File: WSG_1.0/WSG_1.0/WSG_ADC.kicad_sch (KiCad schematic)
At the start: 31 parts, among them J2 USB4110-GF-A, J4 Conn_01x02, U10 TPS22916BYFPR, U11 W25N04KVZEIR, U7 PQ25180YBGT, U8 TPS63802DLAR, U9 TPS7A2025PDBVR

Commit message: finished schematic
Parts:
- added C33: 100nF, symbol Device:C
- added R31: 1M, symbol Device:R
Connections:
- net GND: now also C19.2, C33.2, R31.1
- net VBAT_SENSE: now also C33.1, R31.2
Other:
- moved on the sheet: C19, R26

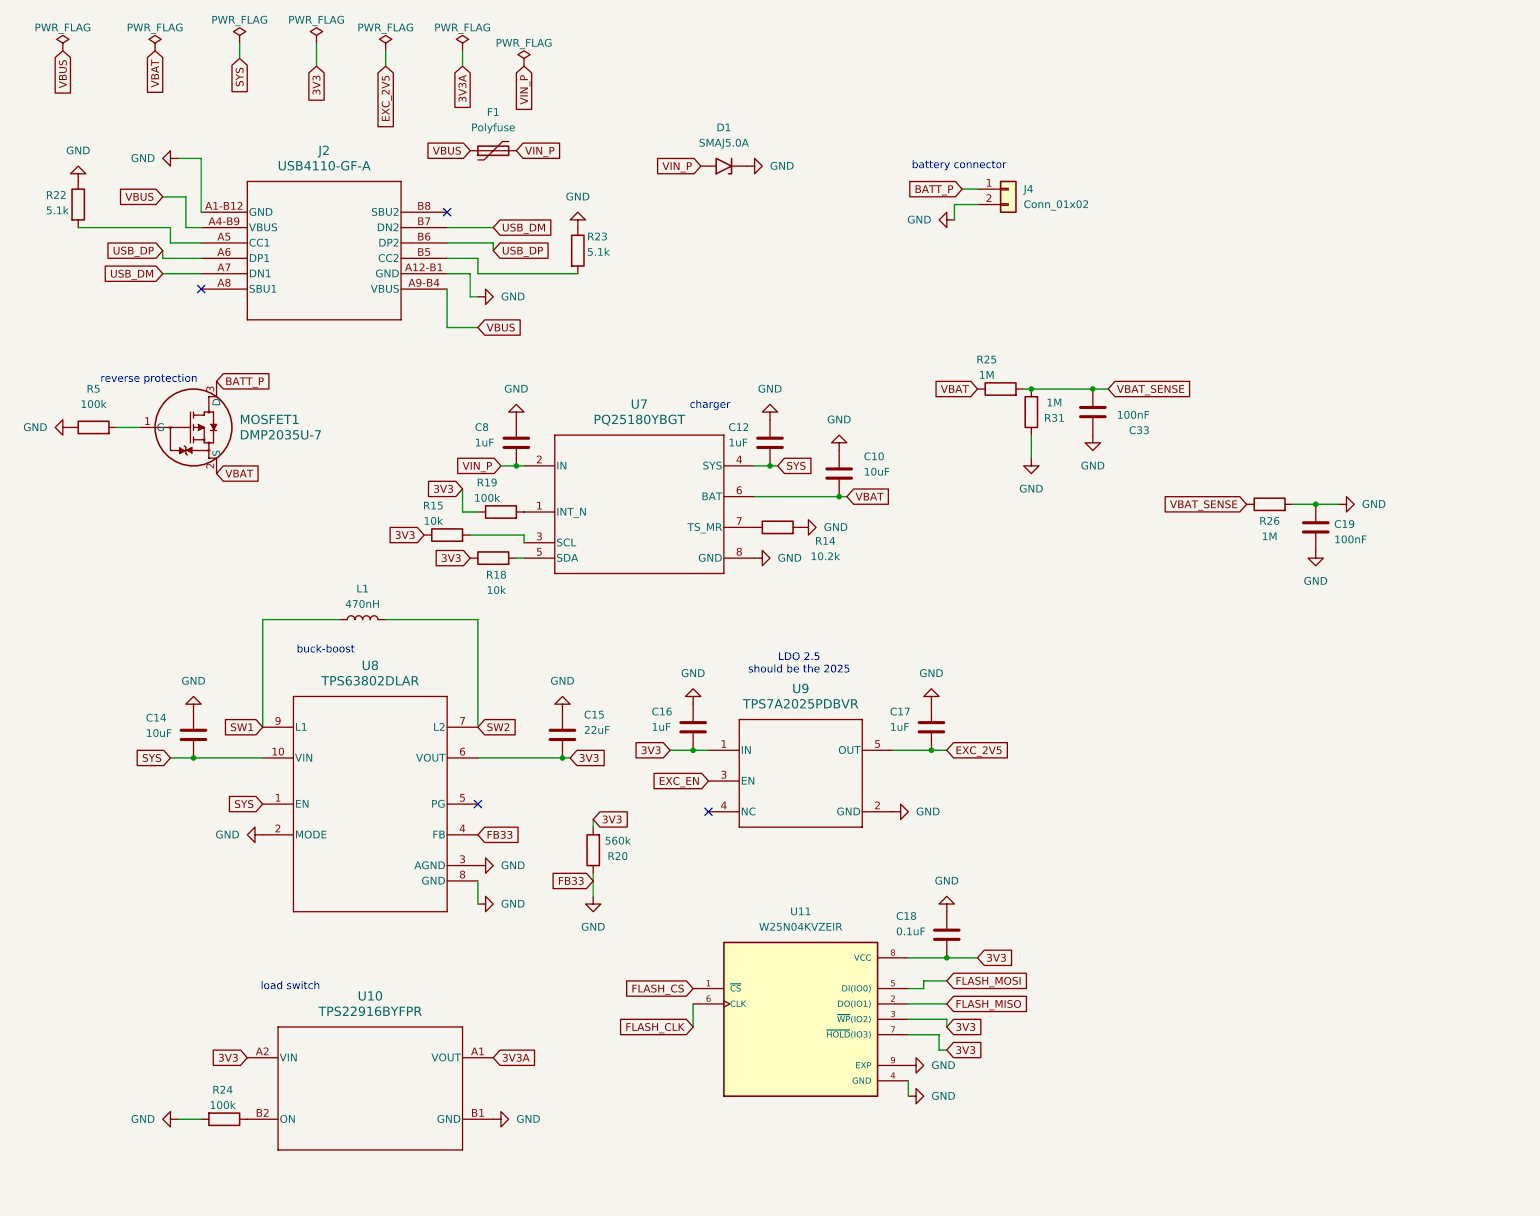
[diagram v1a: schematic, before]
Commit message: added mounting holes, usb esd
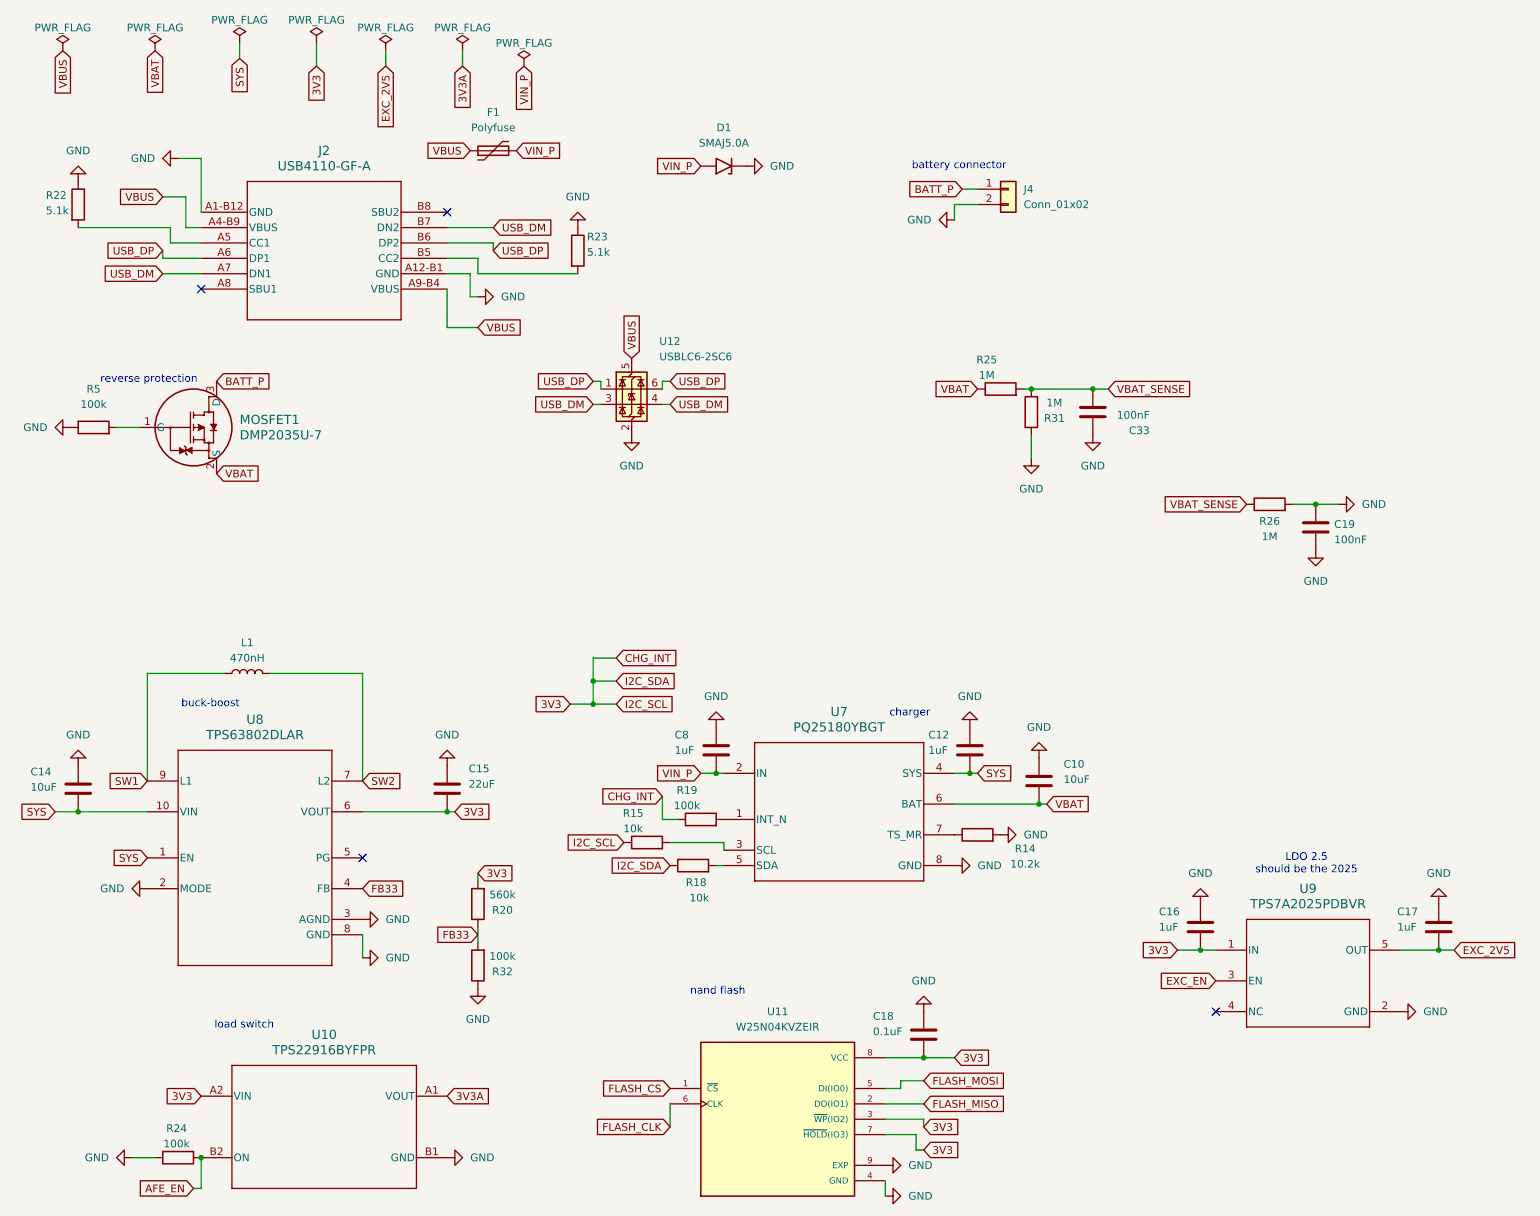
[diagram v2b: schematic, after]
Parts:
- added R32: 100k, symbol Device:R
- added U12: USBLC6-2SC6, Package_TO_SOT_SMD:SOT-23-6, symbol Power_Protection:USBLC6-2SC6
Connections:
- net GND: now also R32.1, U12.2 (GND); no longer R20.1, U8.4 (FB)
- net USB_DM: now also U12.3 (I/O2), U12.4 (I/O2)
- net USB_DP: now also U12.1 (I/O1), U12.6 (I/O1)
- net VBUS: now also U12.5 (VBUS)
- net AFE_EN: now reaches R24.1, U10.B2 (ON)
- new net FB33: R20.1, R32.2, U8.4 (FB)
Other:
- note added: "nand flash"
- moved on the sheet: C10, C12, C14, C15, C16, C17, C18, C8, L1, R14, R15, R18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

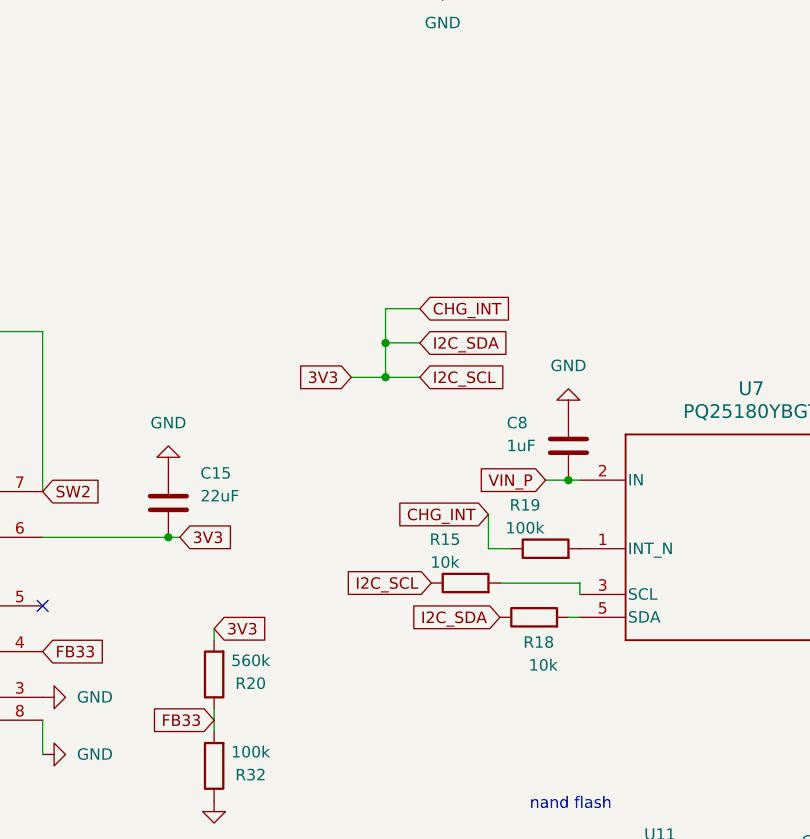
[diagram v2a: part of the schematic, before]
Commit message: fixed combined net labels
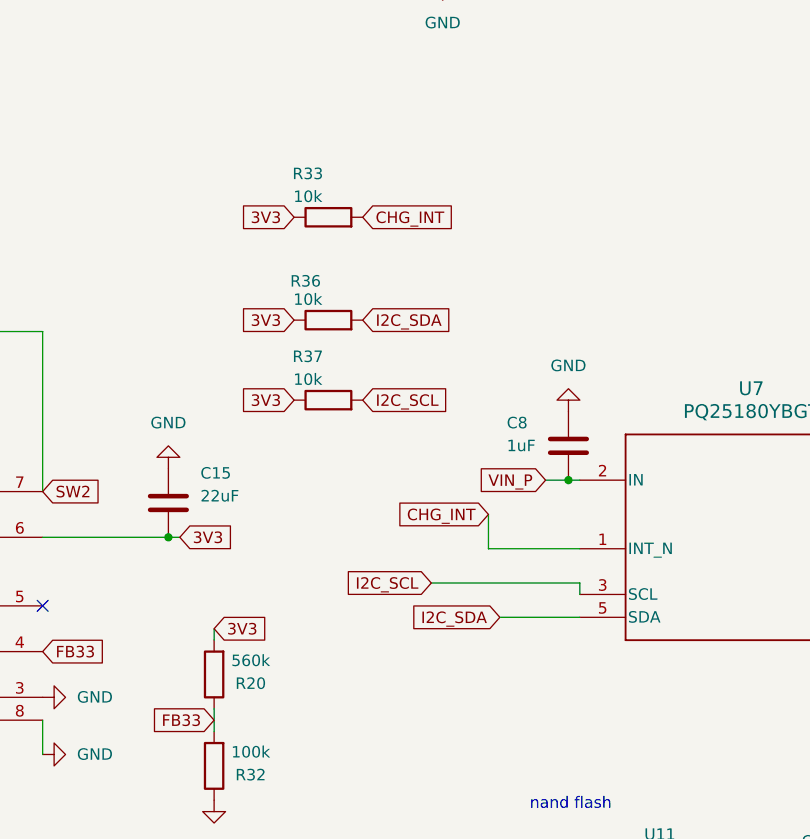
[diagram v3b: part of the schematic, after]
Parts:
- removed R15, R18: 10k, symbol Device:R
- removed R19: 100k, symbol Device:R
- added R33, R36, R37: 10k, symbol Device:R
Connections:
- net 3V3: now also R33.1, R36.1, R37.1
- net I2C_SCL: now reaches U7.3 (SCL)
- net I2C_SCL: now also R37.2
- net CHG_INT: now reaches U7.1 (INT_N)
- net CHG_INT: now also R33.2
- net I2C_SDA: now reaches U7.5 (SDA)
- net I2C_SDA: now also R36.2
